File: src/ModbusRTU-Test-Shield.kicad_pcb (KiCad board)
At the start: 2 copper layers, 68.6 x 53.3 mm, 29 parts, among them J1 Conn_01x08_UNO_Digital_1, J2 Conn_01x10_UNO_Digital_2, J3 Conn_01x08_UNO_Power, J4 Conn_01x06_UNO_Analog, J5 Screw_Terminal_01x03, SW1 SW_Push, SW2 SW_Push, SW3 SW_Push, SW4 SW_DPDT_x2, U1 LT1785AxN8

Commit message: Completed first draft.
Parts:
- added D5: YEL, LED_THT:LED_D3.0mm, F.Cu at (141.0, 102.9)
- added R7: 2K, Resistor_THT:R_Axial_DIN0207_L6.3mm_D2.5mm_P10.16mm_Horizontal, F.Cu at (144.8, 88.9)
- R5: value 1K -> 330
- R6: value 2K -> 1K
- moved D1 37.8 mm to (141.0, 123.2), turned to 0 degrees
- moved D2 30.6 mm to (141.0, 118.1), turned to 0 degrees
- moved R5 26.2 mm to (148.6, 88.9), turned to -90 degrees
- moved D3 23.4 mm to (141.0, 113.0), turned to 0 degrees
- moved R1 23.4 mm to (163.8, 88.9), turned to -90 degrees
- moved R2 18.1 mm to (160.0, 88.9), turned to -90 degrees
- moved D4 16.3 mm to (141.0, 108.0), turned to 0 degrees
- moved R3 12.7 mm to (156.2, 88.9), turned to -90 degrees
- moved R6 10.2 mm to (141.0, 99.1), turned to 90 degrees
- moved C1 8.98 mm to (120.7, 121.9)
- moved U1 8.98 mm to (125.7, 118.1)
- moved SW4 8.13 mm to (124.3, 105.7)
- moved R4 7.41 mm to (152.4, 88.9), turned to -90 degrees
- moved J5 5.08 mm to (113.4, 110.9)
- moved RV1 2.54 mm to (149.9, 121.9)
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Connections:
- D1 pad 1: Net-(D1-K) -> GND
- D1 pad 2: /*5 -> Net-(D1-A)
- D2 pad 1: Net-(D2-K) -> GND
- D2 pad 2: /*6 -> Net-(D2-A)
- D3 pad 1: Net-(D3-K) -> GND
- D3 pad 2: /7 -> Net-(D3-A)
- D4 pad 1: Net-(D4-K) -> GND
- D4 pad 2: /8 -> Net-(D4-A)
- R1 pad 1: Net-(D1-K) -> /*5
- R1 pad 2: GND -> Net-(D1-A)
- R2 pad 1: Net-(D2-K) -> /*6
- R2 pad 2: GND -> Net-(D2-A)
- R3 pad 1: Net-(D3-K) -> /7
- R3 pad 2: GND -> Net-(D3-A)
- R4 pad 1: Net-(D4-K) -> /8
- R4 pad 2: GND -> Net-(D4-A)
- R5 pad 1: Net-(U1-RO) -> /13
- R5 pad 2: Net-(SW4B-B) -> Net-(D5-A)
- R6 pad 1: GND -> Net-(U1-RO)
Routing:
- net Net-(D1-A): track 0.00 -> 38.9 mm
- net Net-(D2-A): track 0.00 -> 30.8 mm
- net /13: track 34.3 -> 61.5 mm
- net Net-(D1-K): track 24.0 -> 0.00 mm
- net Net-(D3-A): track 0.00 -> 22.6 mm
- net Net-(U1-RO): track 3.82 -> 25.4 mm
- net Net-(D2-K): track 17.3 -> 0.00 mm
- net Net-(D4-A): track 0.00 -> 14.5 mm
- net /TX/1: track 46.7 -> 58.9 mm
- net Net-(D3-K): track 10.7 -> 0.00 mm
- net /*3: track 29.2 -> 38.8 mm
- net /RX/0: track 46.8 -> 56.1 mm
- net /*10: track 22.0 -> 30.9 mm
- net /*11: track 24.7 -> 33.3 mm
- net /IOREF: track 34.8 -> 42.9 mm
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
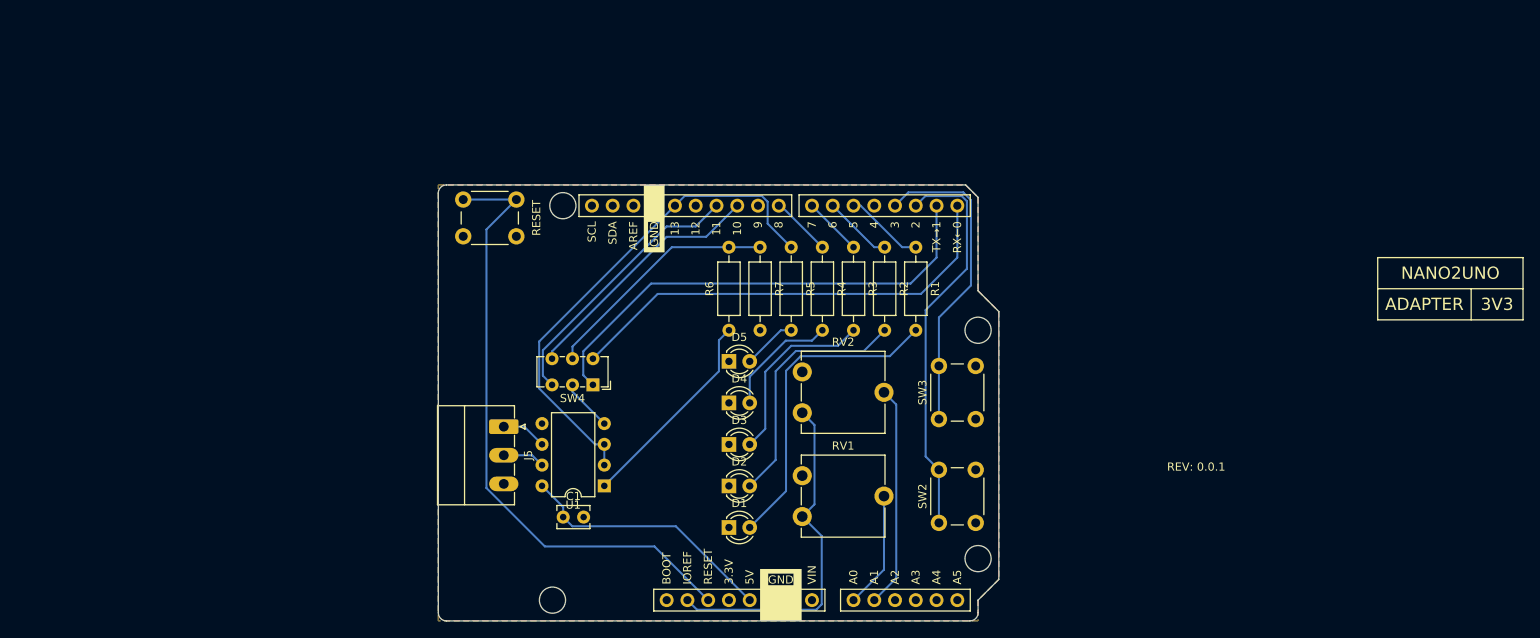
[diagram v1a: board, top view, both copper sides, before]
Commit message: Added RS-232 on an RJ12 connector. Completed second draft.
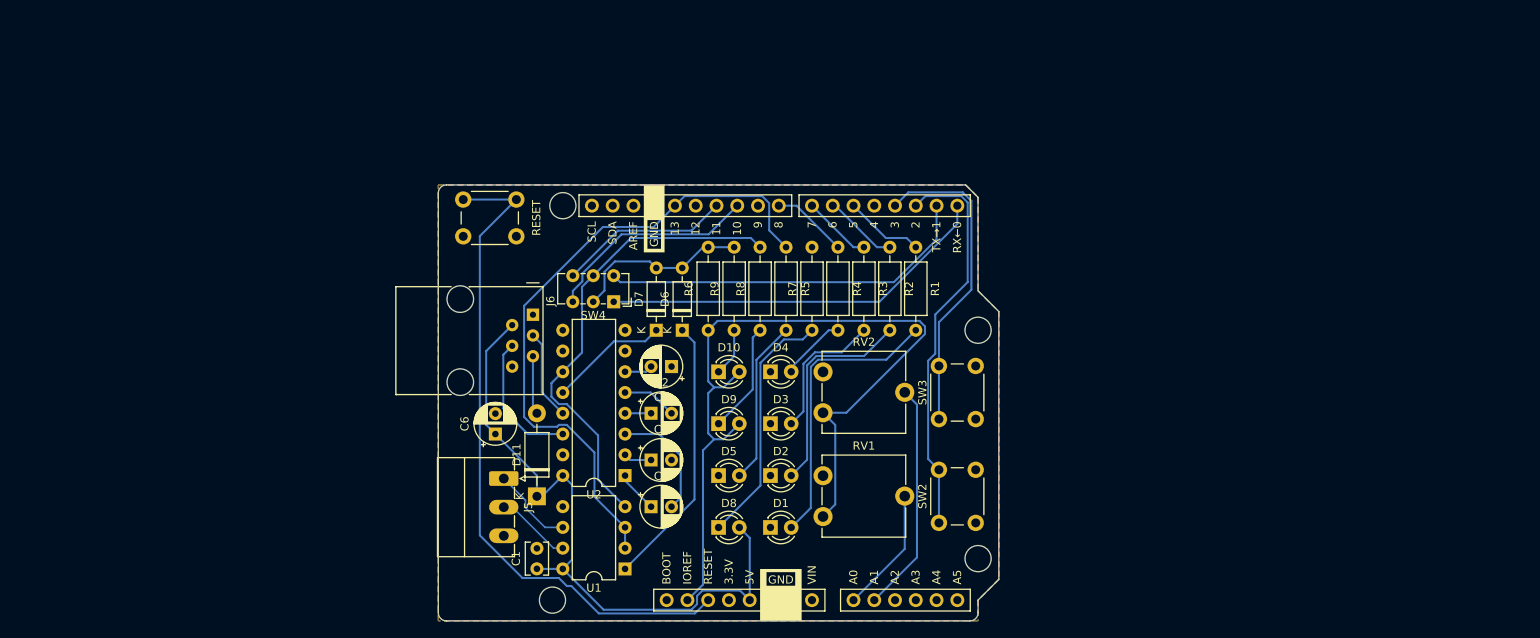
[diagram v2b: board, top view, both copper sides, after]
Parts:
- removed the REF** at (222.2, 111.8)
- added C2: 1uF, Capacitor_THT:CP_Radial_D5.0mm_P2.50mm, F.Cu at (131.4, 109.2)
- added C3: 1uF, Capacitor_THT:CP_Radial_D5.0mm_P2.50mm, F.Cu at (131.4, 120.7)
- added C4: 1uF, Capacitor_THT:CP_Radial_D5.0mm_P2.50mm, F.Cu at (131.4, 114.9)
- added C5: 1uF, Capacitor_THT:CP_Radial_D5.0mm_P2.50mm, F.Cu at (133.9, 103.5)
- added C6: 1uF, Capacitor_THT:CP_Radial_D5.0mm_P2.50mm, F.Cu at (112.4, 111.8)
- added D10: YEL, LED_THT:LED_D3.0mm, F.Cu at (139.7, 104.1)
- added D11: D_Schottky, Diode_THT:D_DO-41_SOD81_P10.16mm_Horizontal, F.Cu at (117.5, 119.4)
- added D6: D_Schottky, Diode_THT:D_DO-35_SOD27_P7.62mm_Horizontal, F.Cu at (135.3, 99.1)
- added D7: D_Schottky, Diode_THT:D_DO-35_SOD27_P7.62mm_Horizontal, F.Cu at (132.1, 99.1)
- added D8: GRN, LED_THT:LED_D3.0mm, F.Cu at (139.7, 123.2)
- added D9: YEL, LED_THT:LED_D3.0mm, F.Cu at (139.7, 110.5)
- added J6: 6P6C, Connector_RJ:RJ12_Amphenol_54601, F.Cu at (117.0, 97.2)
- added R8: 330, Resistor_THT:R_Axial_DIN0207_L6.3mm_D2.5mm_P10.16mm_Horizontal, F.Cu at (144.8, 99.1)
- added R9: 330, Resistor_THT:R_Axial_DIN0207_L6.3mm_D2.5mm_P10.16mm_Horizontal, F.Cu at (141.6, 99.1)
- added REF**: OSHW-Logo_7.5x8mm_SilkScreen, Symbol:OSHW-Logo_7.5x8mm_SilkScreen, B.Cu at (158.1, 112.4)
- added U2: MAX232, Package_DIP:DIP-16_W7.62mm, F.Cu at (128.3, 116.8)
- R6: value 1K -> 10K
- R7: value 2K -> 330
- SW1: value SW_Push -> RESET
- SW2: value SW_Push -> BUTTON1
- SW3: value SW_Push -> BUTTON2
- moved REF** 88.5 mm to (143.5, 94.0)
- moved D5 14.0 mm to (139.7, 116.8)
- moved R7 12.0 mm to (151.1, 99.1), turned to 90 degrees
- moved SW4 10.5 mm to (126.9, 95.6)
- moved U1 10.5 mm to (128.3, 128.3)
- moved C1 7.10 mm to (117.5, 128.2), turned to 90 degrees
- moved D4 6.35 mm to (146.1, 104.1)
- moved J5 6.35 mm to (113.4, 117.2)
- moved D3 5.68 mm to (146.1, 110.5)
- moved D2 5.24 mm to (146.1, 116.8)
- moved D1 5.08 mm to (146.1, 123.2)
- moved R6 2.54 mm to (138.4, 99.1)
- moved RV1 2.54 mm to (152.5, 121.9)
- moved RV2 2.54 mm to (152.5, 109.2)
- moved R4 1.91 mm to (154.3, 88.9)
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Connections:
- net /*3 renamed /BUTTON1
- net /*5 renamed /LED4
- net /*6 renamed /LED3
- net /13 renamed /DE
- net /2 renamed /BUTTON2
- net /7 renamed /LED2
- net /8 renamed /LED1
- net /A0 renamed /POT1
- net /A1 renamed /POT2
- net Net-(J3-RESET) renamed /RESET
- net Net-(J5-Pin_1) renamed /RS485_D+
- net Net-(J5-Pin_2) renamed /RS485_D-
- J1 pad 1: /RX/0 -> /HARD_RX
- J1 pad 2: /TX/1 -> /HARD_TX
- J2 pad 3: /*10 -> /SOFT_RX
- J2 pad 4: /*11 -> /SOFT_TX
- R6 pad 1: Net-(U1-RO) -> /IOREF
- R6 pad 2: Net-(SW4B-B) -> /RX
- R7 pad 1: Net-(SW4B-B) -> Net-(D8-K)
- SW4 pad 1: /TX/1 -> /HARD_RX
- SW4 pad 2: Net-(SW4A-B) -> /RX
- SW4 pad 3: /*11 -> /SOFT_RX
- SW4 pad 4: /RX/0 -> /HARD_TX
- SW4 pad 5: Net-(SW4B-B) -> /TX
- SW4 pad 6: /*10 -> /SOFT_TX
- U1 pad 1: Net-(U1-RO) -> Net-(D6-K)
- U1 pad 4: Net-(SW4A-B) -> /TX
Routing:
- net /TX/1: track 58.9 -> 0.00 mm
- net /IOREF: track 42.9 -> 101.6 mm
- net /TX: track 0.00 -> 57.5 mm
- net /RX/0: track 56.1 -> 0.00 mm
- net +5V: track 31.9 -> 81.0 mm
- net /HARD_RX: track 0.00 -> 48.2 mm
- net /HARD_TX: track 0.00 -> 46.1 mm
- net Net-(D6-K): track 0.00 -> 33.3 mm
- net /*11: track 33.3 -> 0.00 mm
- net /*10: track 30.9 -> 0.00 mm
- net Net-(D8-K): track 0.00 -> 30.2 mm
- net Net-(SW4B-B): track 29.5 -> 0.00 mm
- net /SOFT_RX: track 0.00 -> 26.3 mm
- net Net-(U1-RO): track 25.4 -> 0.00 mm
- net /RX: track 0.00 -> 22.0 mm
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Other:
- board text added: "Circuit Board Specifications Board Thickness: 1.6mm Substrate Material: FR4 Copper Layers: 2 Copper Thickness: 1oz Soldermask Color: Any (Blue Suggested) Surface Finish: Any (HASL Lead-Free Suggested) Smallest Hole Diameter: 0.8mm Smallest Trace Width: 0.2mm (7.8mil) Smallest Trace Spacing: 0.2mm (7.8mil) Documentation and source files can be found at https://github.com/CMB27/ModbusRTU-Test-Shiel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"
- board text added: "MODBUS RTU"
- board text added: "TEST SHIELD"
- board text removed: "3V3"
- board text removed: "ADAPTER"
- board text removed: "Circuit Board Specifications Board Thickness: 1.6mm Substrate Material: FR4 Copper Layers: 2 Copper Thickness: 1oz Soldermask Color: Any (Blue Suggested) Surface Finish: Any (HASL Lead-Free Suggested) Smallest Hole Diameter: 0.8mm Smallest Trace Width: 0.2mm (7.8mil) Smallest Trace Spacing: 0.2mm (7.8mil) Documentation and source files can be found at https://github.com/CMB27/Nano2UNO-Adapter-3V3."
- board text removed: "NANO2UNO"

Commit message: Added some 3D models. Created project footprints for RJ12 and screw terminal connectors. Placed and locked RJ12 and screw terminal connector.
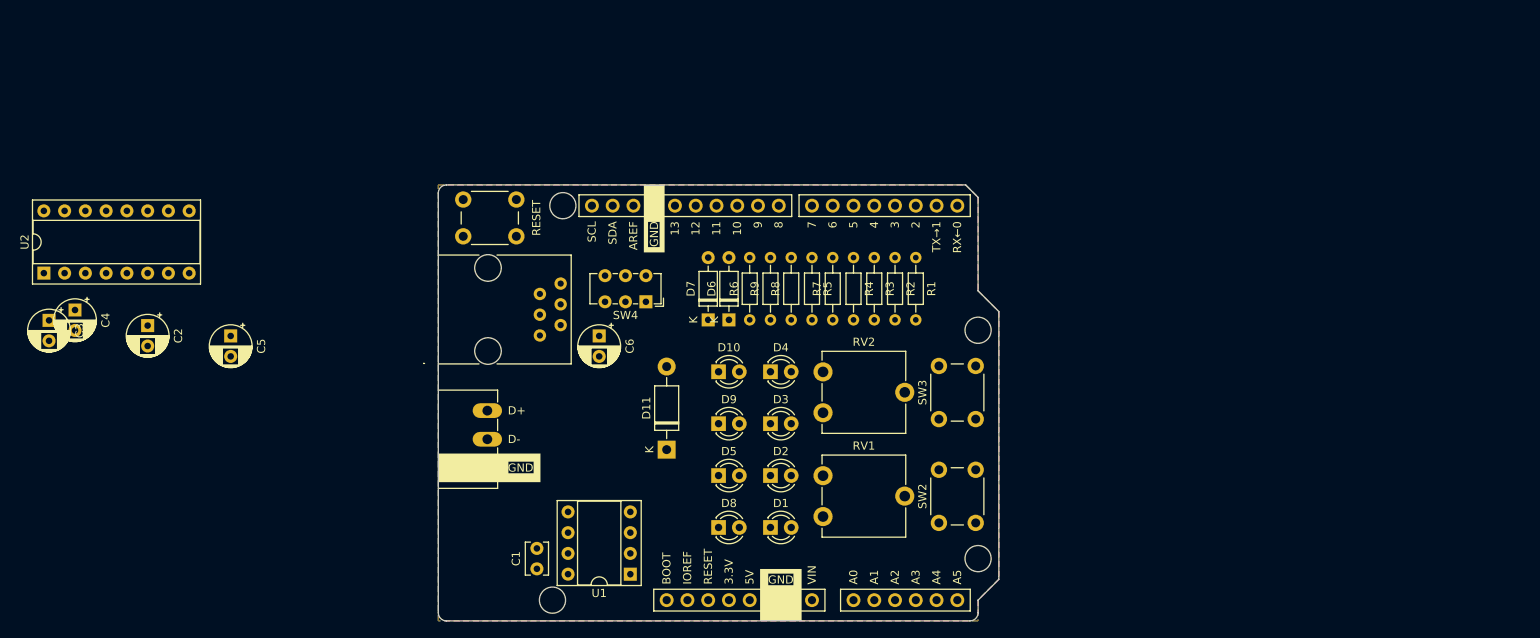
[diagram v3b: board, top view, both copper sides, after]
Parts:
- J5: footprint Connector_Phoenix_MC:PhoenixContact_MC_1,5_3-G-3.5_1x03_P3.50mm_Horizontal -> Project_Footprints:PhoenixContact_BCH-350H-3_RS485
- J6: footprint Connector_RJ:RJ12_Amphenol_54601 -> Project_Footprints:FCI_54601-906WPLF
- R1, R2, R3, R4, R5, R6, R7, R8, R9: footprint Resistor_THT:R_Axial_DIN0207_L6.3mm_D2.5mm_P10.16mm_Horizontal -> Resistor_THT:R_Axial_DIN0204_L3.6mm_D1.6mm_P7.62mm_Horizontal
- U1: footprint Package_DIP:DIP-8_W7.62mm -> Package_DIP:DIP-8_W7.62mm_Socket
- U2: footprint Package_DIP:DIP-16_W7.62mm -> Package_DIP:DIP-16_W7.62mm_Socket
- moved C3 77.1 mm to (57.8, 97.9), turned to -90 degrees
- moved U2 75.3 mm to (57.1, 92.1), turned to 90 degrees
- moved C4 72.8 mm to (61.0, 96.6), turned to -90 degrees
- moved C2 62.5 mm to (69.8, 98.5), turned to -90 degrees
- moved REF** 59.7 mm to (203.2, 95.2)
- moved C5 54.1 mm to (80.0, 99.8), turned to -90 degrees
- moved REF** 40.7 mm to (198.1, 104.8)
- moved C6 17.5 mm to (125.1, 99.8), turned to -90 degrees
- moved D11 16.9 mm to (133.3, 113.7)
- moved J6 11.6 mm to (105.4, 96.5)
- moved J5 9.35 mm to (105.4, 112.4)
- moved D7 6.48 mm to (138.4, 97.8)
- moved D6 5.85 mm to (141.0, 97.8)
- moved R6 5.24 mm to (143.5, 97.8)
- moved R9 4.62 mm to (146.1, 97.8)
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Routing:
- net /IOREF: track 101.6 -> 0.00 mm
- net /RESET: track 82.0 -> 0.00 mm
- net +5V: track 81.0 -> 0.00 mm
- net /DE: track 79.6 -> 0.00 mm
- net /TX: track 57.5 -> 0.00 mm
- net /BUTTON2: track 48.9 -> 0.00 mm
- net /HARD_RX: track 48.2 -> 0.00 mm
- net /HARD_TX: track 46.1 -> 0.00 mm
- net /BUTTON1: track 38.8 -> 0.00 mm
- net Net-(D1-A): track 35.3 -> 0.00 mm
- net Net-(D6-K): track 33.3 -> 0.00 mm
- net Net-(D8-K): track 30.2 -> 0.00 mm
- net /POT2: track 28.2 -> 0.00 mm
- net /SOFT_RX: track 26.3 -> 0.00 mm
- net Net-(D2-A): track 26.2 -> 0.00 mm
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
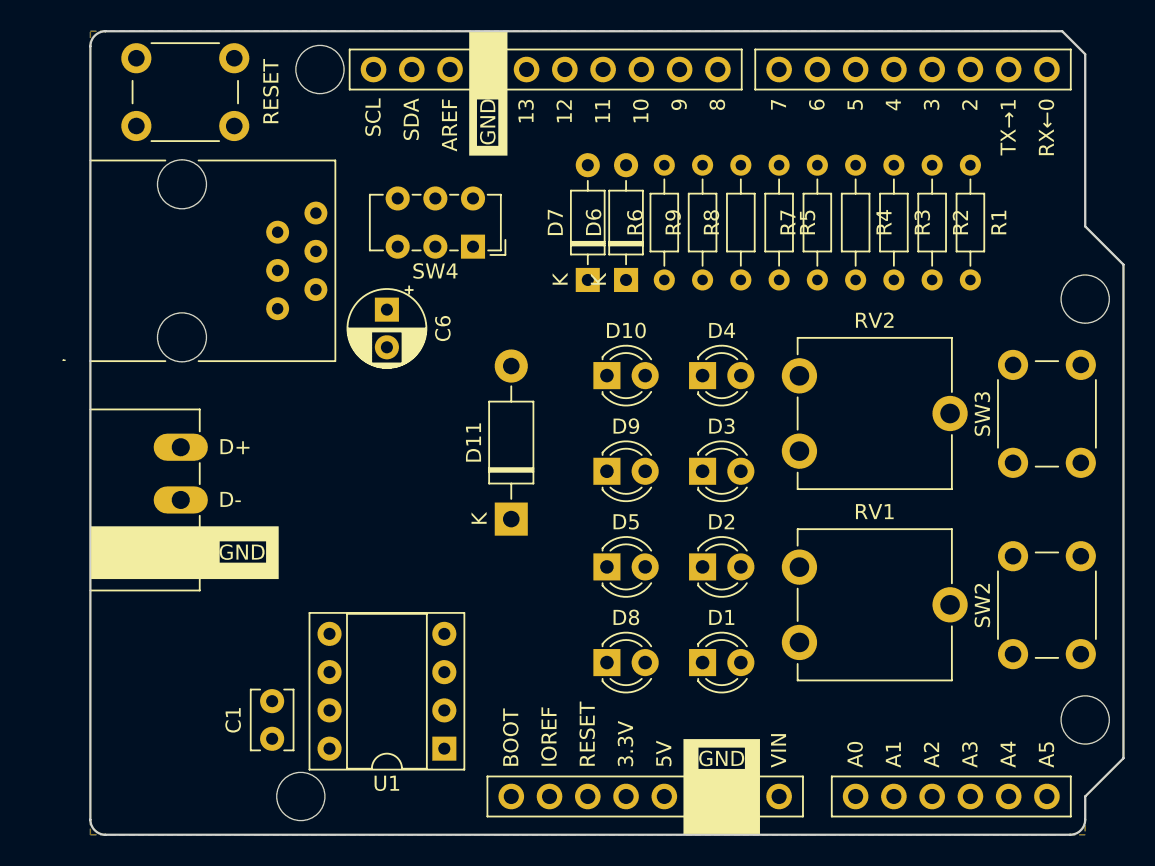
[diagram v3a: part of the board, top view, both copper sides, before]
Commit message: Refined button footprints. Updated and refined potentiometer footprints and models.
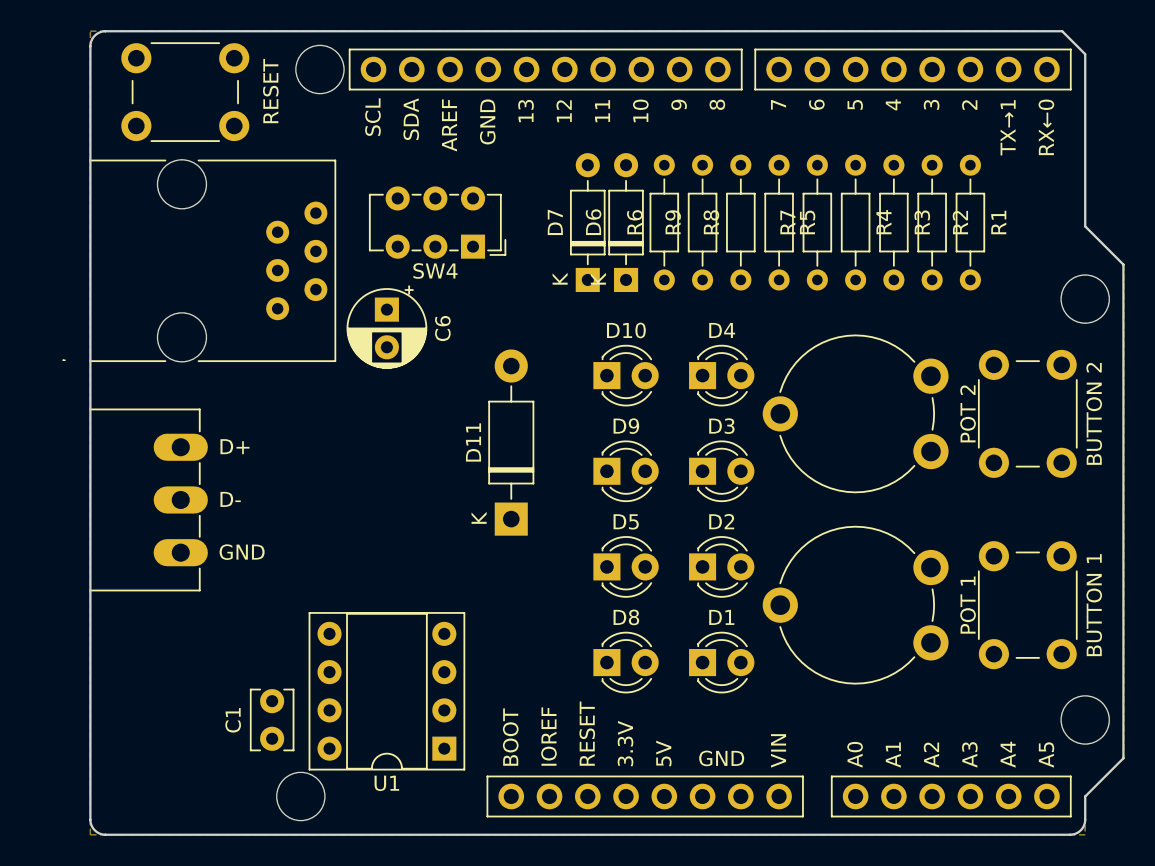
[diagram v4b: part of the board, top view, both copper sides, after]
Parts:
- RV1, RV2: footprint Potentiometer_THT:Potentiometer_ACP_CA9-V10_Vertical -> Project_Footprints:Potentiometer_Piher_PT-10-V10_Vertical
- SW1: footprint Project_Footprints:SW_PUSH_6mm_Reset -> Project_Footprints:SW_PUSH_6mm
- SW2, SW3: footprint Button_Switch_THT:SW_PUSH_6mm -> Project_Footprints:SW_PUSH_6mm
- moved RV1 4.48 mm to (156.2, 119.4), turned to 90 degrees
- moved RV2 4.48 mm to (156.2, 106.7), turned to 90 degrees
- moved SW2 3.39 mm to (167.6, 119.4)
- moved SW3 3.39 mm to (167.6, 106.7)
